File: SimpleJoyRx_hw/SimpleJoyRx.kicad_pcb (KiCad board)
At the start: 4 copper layers, 24 x 90 mm, 113 parts, among them Q1 IRF9358, Q2 2N7002, Q3 IRLML0030, Q4 IRLML0030, SW1 DIPx8, SW2 BUTTON, SW3 1P2T, U1 USBLC6

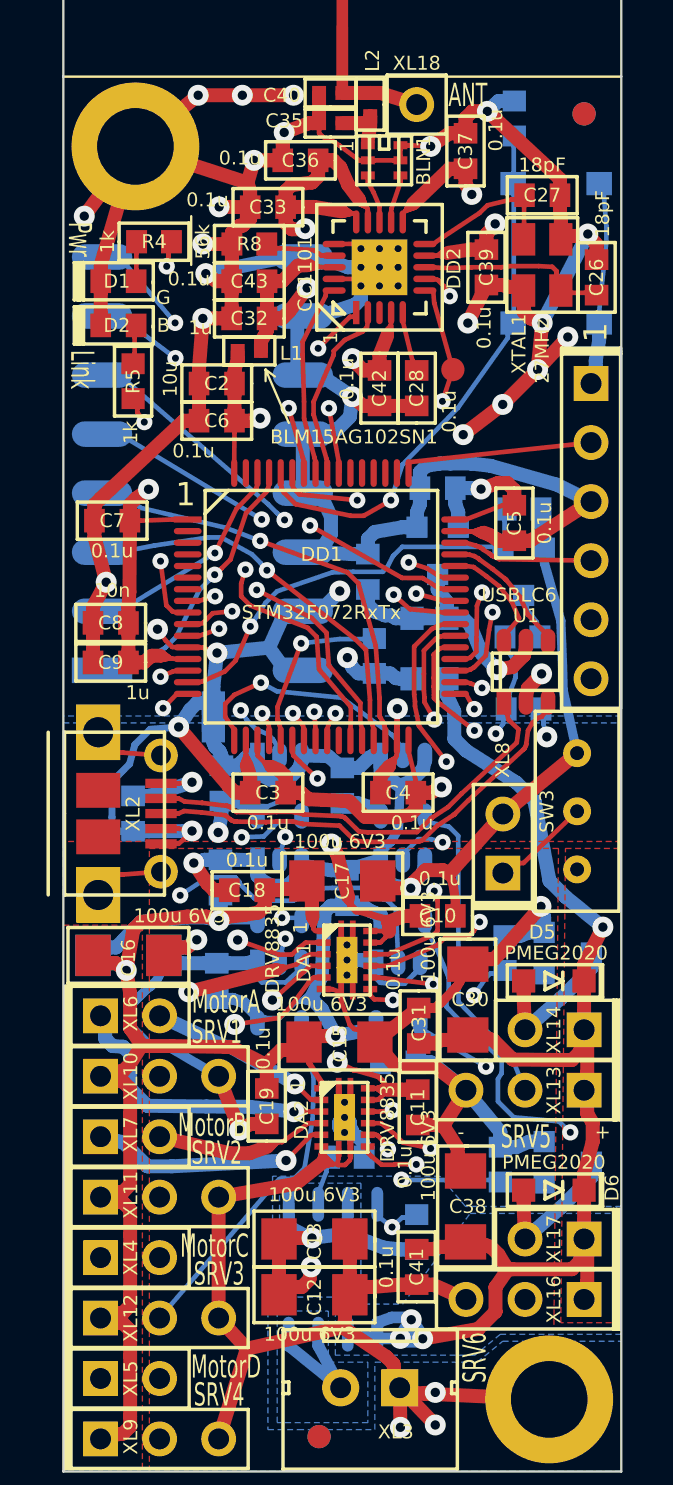
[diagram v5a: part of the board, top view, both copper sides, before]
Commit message: + SimpleJoy TX * Leg 63 bug fixed
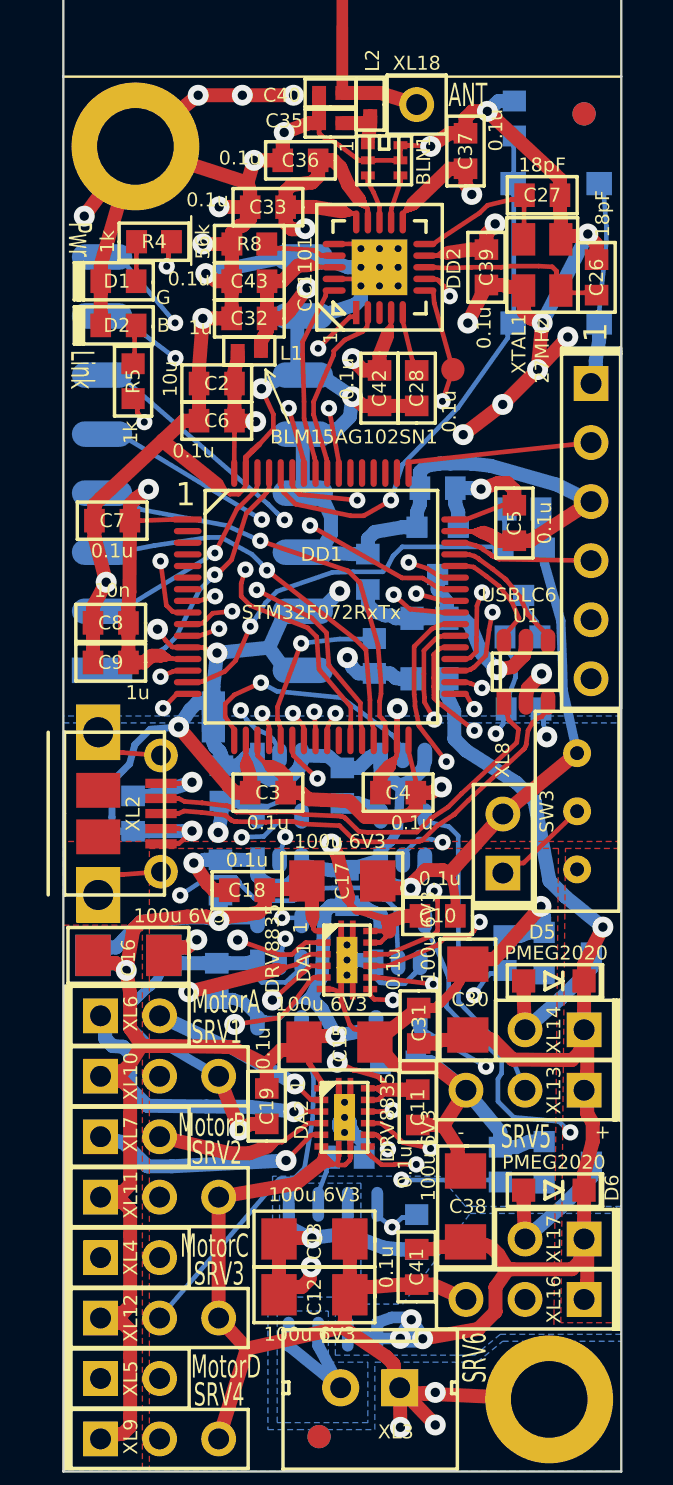
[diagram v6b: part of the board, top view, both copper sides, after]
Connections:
- DD1 pad 2: Net-(DD1-Pad2) -> (no net)
- DD1 pad 26: Net-(DD1-Pad26) -> (no net)
- DD1 pad 3: Net-(DD1-Pad3) -> (no net)
- DD1 pad 4: Net-(DD1-Pad4) -> (no net)
- DD1 pad 5: Net-(DD1-Pad5) -> (no net)
- DD1 pad 50: Net-(DD1-Pad50) -> (no net)
- DD1 pad 51: Net-(DD1-Pad51) -> (no net)
- DD1 pad 52: Net-(DD1-Pad52) -> (no net)
- DD1 pad 53: Net-(DD1-Pad53) -> (no net)
- DD1 pad 54: Net-(DD1-Pad54) -> (no net)
- DD1 pad 6: Net-(DD1-Pad6) -> (no net)
- DD1 pad 63: (no net) -> GND
- DD1 pad 7: Net-(DD1-Pad7) -> (no net)
- DD2 pad 3: (no net) -> Net-(DD2-Pad3)
- SW3 pad 3: (no net) -> Net-(SW3-Pad3)
- XL2 pad H2: Net-(XL2-PadH2) -> (no net)
- XL2 pad H3: Net-(XL2-PadH3) -> (no net)
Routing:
- net GND: track 214.3 -> 228.1 mm, vias 28 -> 29
- net PwrUnst: track 210.0 -> 213.1 mm
- net VCC: track 60.0 -> 62.6 mm
- net +3.3V: track 123.1 -> 124.3 mm
- net GNDPWR: track 194.9 -> 196.0 mm
- net /MOTORB1: track 9.14 -> 10.0 mm
- net /MOTORC2: track 22.4 -> 23.2 mm

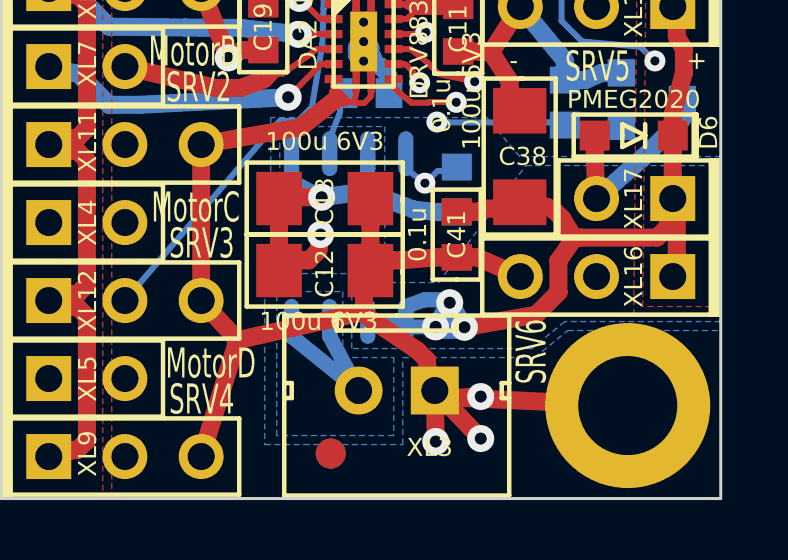
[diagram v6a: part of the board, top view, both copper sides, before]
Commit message: TX: USB and switch moved to edges. Sent to production.
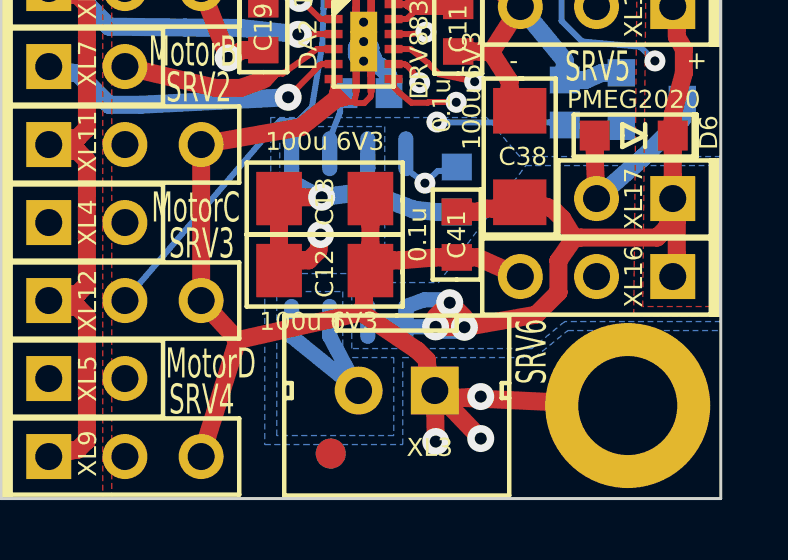
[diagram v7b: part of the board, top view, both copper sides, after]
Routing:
- net PwrUnst: track 213.1 -> 216.5 mm
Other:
- rule pad_to_mask_clearance: 0 -> 0.1
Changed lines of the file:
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@@
     (thickness 1.6)
     (drawings 60)
-    (tracks 2914)
+    (tracks 2921)
     (zones 0)
     (modules 113)
@@
     (pad_size 1.5 1.5)
     (pad_drill 0.6)
-    (pad_to_mask_clearance 0)
+    (pad_to_mask_clearance 0.1)
+    (solder_mask_min_width 0.15)
     (aux_axis_origin 0 0)
     (visible_elements 7FFFF27F)
     (pcbplotparams
-      (layerselection 0x00030_ffffffff)
-      (usegerberextensions false)
+      (layerselection 0x010f0_ffffffff)
+      (usegerberextensions true)
       (usegerberattributes true)
       (usegerberadvancedattributes true)
@@
       (outputformat 1)
       (mirror false)
-      (drillshape 1)
+      (drillshape 0)
       (scaleselection 1)
-      (outputdirectory ""))
+      (outputdirectory Gerber))
   )
   (net 0 "")
@@
   (segment (start 134.588 121.739) (end 134.266 122.061) (width 0.6) (layer F.Cu) (net 9))
   (segment (start 134.66 121.2) (end 134.588 121.739) (width 0.6) (layer F.Cu) (net 9))
+  (segment (start 139.456 124.291) (end 139.456 123.962) (width 0.6) (layer In2.Cu) (net 10))
+  (segment (start 139.456 123.962) (end 138.966 123.472) (width 0.6) (layer In2.Cu) (net 10))
+  (segment (start 138.495 124.277) (end 138.495 123.943) (width 0.6) (layer In2.Cu) (net 10))
+  (segment (start 138.495 123.943) (end 138.966 123.472) (width 0.6) (layer In2.Cu) (net 10))
+  (segment (start 139.456 124.291) (end 138.509 124.291) (width 0.6) (layer In2.Cu) (net 10))
+  (segment (start 139.456 123.962) (end 138.966 123.472) (width 0.6) (layer F.Cu) (net 10))
+  (segment (start 138.495 123.943) (end 138.966 123.472) (width 0.6) (layer F.Cu) (net 10))
+  (segment (start 139.456 124.291) (end 138.509 124.291) (width 0.6) (layer F.Cu) (net 10))
+  (segment (start 138.509 124.291) (end 138.495 124.277) (width 0.6) (layer F.Cu) (net 10))
   (via (at 135.716 111.273) (size 0.9) (drill 0.4) (layers F.Cu B.Cu) (net 10))
   (via (at 126.708 108.446) (size 0.9) (drill 0.4) (layers F.Cu B.Cu) (net 10))
@@
   (segment (start 139.34 124.374) (end 138.592 124.374) (width 0.6) (layer B.Cu) (net 10))
   (segment (start 139.456 124.291) (end 139.34 124.374) (width 0.6) (layer B.Cu) (net 10))
-  (segment (start 139.456 124.291) (end 138.966 123.472) (width 0.6) (layer B.Cu) (net 10))
   (segment (start 132.35 110.468) (end 132.35 110.496) (width 0.5) (layer B.Cu) (net 10))
   (segment (start 132.314 110.379) (end 132.35 110.468) (width 0.5) (layer B.Cu) (net 10))
@@
   (segment (start 137.505 123.597) (end 137.505 124.094) (width 0.5) (layer B.Cu) (net 10))
   (segment (start 138.121 123.375) (end 137.505 123.597) (width 0.5) (layer B.Cu) (net 10))
-  (segment (start 138.869 123.375) (end 138.121 123.375) (width 0.5) (layer B.Cu) (net 10))
   (segment (start 138.966 123.472) (end 138.869 123.375) (width 0.5) (layer B.Cu) (net 10))
+  (segment (start 138.869 123.375) (end 138.121 123.375) (width 0.5) (layer B.Cu) (net 10))
   (segment (start 137.638 112.192) (end 137.638 112.4) (width 0.6) (layer B.Cu) (net 10))
   (segment (start 137.638 111.892) (end 137.638 112.192) (width 0.6) (layer B.Cu) (net 10))
@@
   (segment (start 137.505 124.277) (end 137.505 124.094) (width 0.5) (layer B.Cu) (net 10))
   (segment (start 138.495 124.277) (end 137.505 124.277) (width 0.5) (layer B.Cu) (net 10))
-  (segment (start 138.495 124.277) (end 138.966 123.472) (width 0.6) (layer B.Cu) (net 10))
   (segment (start 134.523 109.492) (end 134.188 109.77) (width 0.2) (layer B.Cu) (net 10))
   (segment (start 134.187 109.77) (end 134.523 109.492) (width 0.2) (layer B.Cu) (net 10))

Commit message: + RX v2
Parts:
- removed C22, C23, C29, C34: 0.1u, Capacitors:CAP_0603
- removed DA4, DA5, DA6, DA8, DA9: MC74VHC1, SOT:SOT23-5
- added XL15: PLS3, Connectors:PLS-3, F.Cu at (141.4, 125.8)
- added XL19: PLS3, Connectors:PLS-3, F.Cu at (141.4, 133.0)
- added XL20: PLS3, Connectors:PLS-3, F.Cu at (141.4, 128.4)
- added XL21: PLS3, Connectors:PLS-3, F.Cu at (141.4, 135.6)
- C12, C17, C31, D5, D6: moved to B.Cu
- C35: value * -> 2.4pF
- C40: value * -> DoNotMount
- DA3: value MC74VHC1 -> MCP1700; footprint SOT:SOT23-5 -> SOT:SOT23-3A
- DA7: footprint SOT:SOT23-3 -> SOT:SOT23-3A
- L2: value * -> 1.2nH
- Q3, Q4, R1, R11, R12: moved to F.Cu
- SW2: value BUTTON -> IT-1187A
- XL8: value CONN_2 -> PLS2
- moved C20 15.4 mm to (136.3, 97.1)
- moved HOLE2 11.3 mm to (136.0, 133.8)
- moved C19 9.93 mm to (131.8, 104.4), turned to 270 degrees
- moved DA3 9.78 mm to (136.5, 99.8), turned to 90 degrees
- moved C11 9.74 mm to (138.9, 104.6), turned to 270 degrees
- moved C14 9.17 mm to (135.7, 110.0)
- moved C16 9.17 mm to (135.7, 110.0)
- moved C21 8.65 mm to (139.4, 99.8)
- moved XL9 8.60 mm to (130.6, 135.6), turned to 180 degrees
- moved DA2 7.98 mm to (135.6, 106.8)
- moved C15 7.94 mm to (135.4, 103.6)
- moved XL5 7.47 mm to (128.2, 133.0), turned to 180 degrees
- moved XL12 6.93 mm to (130.6, 128.2), turned to 180 degrees
- moved C12 6.69 mm to (131.0, 116.9), turned to 270 degrees
- moved R1 6.18 mm to (133.4, 122.0), turned to 270 degrees
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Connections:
- C20 pad 1: PwrUnst -> /MCU_PWR
- C20 pad 2: GNDPWR -> GND
- C21 pad 1: PwrUnst -> VAA
- C21 pad 2: GNDPWR -> GND
- C32 pad 1: VCC -> GND
- C32 pad 2: GND -> VCC
- DA3 pad 1: GNDPWR -> GND
- DA3 pad 2: /SRV4 -> VAA
- DA3 pad 3: GNDPWR -> /MCU_PWR
- DD1 pad 10: /DIR1 -> /A1
- DD1 pad 11: /DIR2 -> /A2
- DD1 pad 2: (no net) -> /DIR4
- DD1 pad 24: /DIR3 -> /A3
- DD1 pad 25: /DIR4 -> /A4
- DD1 pad 51: (no net) -> /DIR1
- DD1 pad 52: (no net) -> /DIR2
- DD1 pad 53: (no net) -> /DIR3
- R10 pad 1: /BAT_MEAS -> Net-(Q2-Pad3)
- R10 pad 2: Net-(Q2-Pad3) -> /BAT_MEAS
- R9 pad 1: +BATT -> /BAT_MEAS
- R9 pad 2: /BAT_MEAS -> +BATT
- XL10 pad 1: PwrUnst -> /SRV1
- XL10 pad 2: Net-(DA4-Pad4) -> PwrUnst
- XL11 pad 1: PwrUnst -> /SRV2
- XL11 pad 2: Net-(DA5-Pad4) -> PwrUnst
- XL12 pad 1: PwrUnst -> /SRV3
- XL12 pad 2: Net-(DA6-Pad4) -> PwrUnst
- XL13 pad 1: PwrUnst -> /SRV5
- XL13 pad 2: Net-(DA8-Pad4) -> PwrUnst
- XL16 pad 1: PwrUnst -> /SRV6
- XL16 pad 2: Net-(DA9-Pad4) -> PwrUnst
- XL9 pad 1: PwrUnst -> /SRV4
- XL9 pad 2: Net-(DA3-Pad4) -> PwrUnst
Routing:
- net PwrUnst: track 216.5 -> 115.0 mm, vias 8 -> 9
- net /A3: track 0.00 -> 45.1 mm, vias 0 -> 1
- net /A4: track 0.00 -> 43.4 mm, vias 0 -> 1
- net /A2: track 0.00 -> 42.8 mm, vias 0 -> 1
- net /A1: track 0.00 -> 40.5 mm, vias 0 -> 1
- net VAA: track 0.00 -> 39.0 mm
- net /ANT2: track 6.12 -> 38.6 mm
- net Net-(DA3-Pad4): track 25.4 -> 0.00 mm, vias 1 -> 0
- net /DIR4: track 17.2 -> 40.8 mm, vias 2 -> 3
- net /SRV3: track 25.1 -> 48.4 mm, vias 2 -> 1
- net Net-(DA9-Pad4): track 20.2 -> 0.00 mm, vias 1 -> 0
- net /SRV1: track 15.1 -> 35.0 mm, vias 2 -> 1
- net /SRV5: track 10.8 -> 30.3 mm, vias 1 -> 2
- net /SRV4: track 24.0 -> 41.6 mm, vias 2 -> 1
- net /SRV2: track 23.3 -> 39.1 mm, vias 2 -> 1
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- removed copper zone on In2.Cu, net GNDPWR
- removed copper zone on F.Cu, net PwrUnst
- removed copper zone on In1.Cu, net PwrUnst
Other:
- board size 24 x 90 mm -> 24 x 97 mm
- net class Default: clearance 0.21 -> 0.15
- net class Wide: clearance 0.21 -> 0.15
- net class Wide05 removed
- rule trace_clearance: 0.21 -> 0.15
- board text added: "1"
- board text added: "2"
- board text added: "3"
- board text added: "4"
- board text added: "5"
- board text added: "6"
- board text added: "A1"
- board text added: "A2"
- board text added: "A3"
- board text added: "A4"
- board text added: "SimpleJoy RX 2.0"
- board text removed: "MotorA"
- board text removed: "MotorB"
- board text removed: "MotorC"
- board text removed: "MotorD"
- board text removed: "PWM5"
- board text removed: "PWM6"
- board text removed: "SRV5"
- board text removed: "SRV6"
- board text removed: "SimpleJoy RX 1.0"
